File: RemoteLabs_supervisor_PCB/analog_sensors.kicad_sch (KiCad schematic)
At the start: 12 parts

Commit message: adding test sketch
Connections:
- net 5V_IN renamed VCC
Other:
- moved on the sheet: C?
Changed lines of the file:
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@@
     (stroke (width 0) (type default) (color 0 0 0 0))
   )
-  (wire (pts (xy 121.92 101.6) (xy 121.92 104.14))
+  (wire (pts (xy 121.92 102.87) (xy 121.92 104.14))
     (stroke (width 0) (type default) (color 0 0 0 0))
   )
@@
   )
   (wire (pts (xy 135.89 69.85) (xy 139.7 69.85))
+    (stroke (width 0) (type default) (color 0 0 0 0))
+  )
+  (wire (pts (xy 121.92 95.25) (xy 121.92 93.98))
     (stroke (width 0) (type default) (color 0 0 0 0))
   )
@@
     (effects (font (size 1.27 1.27)) (justify left bottom))
   )
-  (hierarchical_label "5V_IN" (shape input) (at 118.11 53.34 90)
+  (hierarchical_label "VCC" (shape input) (at 118.11 53.34 90)
     (effects (font (size 1.27 1.27)) (justify left))
   )
@@
     (pin "8")
   )
-  (symbol (lib_id "000_Capacitor_Film_Immo:cap_film_0805") (at 121.92 97.79 0) (unit 1)
-    (in_bom yes) (on_board yes) (fields_autoplaced)
-    (property "Reference" "C?" (id 0) (at 125.73 96.5199 0)
-      (effects (font (size 1.27 1.27)) (justify left))
-    )
-    (property "Value" "100n" (id 1) (at 125.73 99.0599 0)
-      (effects (font (size 1.27 1.27)) (justify left))
-    )
-    (property "Footprint" "Capacitor_SMD:C_0805_2012Metric_Pad1.18x1.45mm_HandSolder" (id 2) (at 123.19 107.95 0)
-      (effects (font (size 1.27 1.27)) hide)
-    )
-    (property "Datasheet" "~" (id 3) (at 121.92 97.79 0)
-      (effects (font (size 1.27 1.27)) hide)
-    )
+  (symbol (lib_id "000_Capacitor_Film_Immo:cap_film_0805") (at 121.92 99.06 0) (unit 1)
+    (in_bom yes) (on_board yes) (fields_autoplaced)
+    (property "Reference" "C?" (id 0) (at 125.73 97.7899 0)
+      (effects (font (size 1.27 1.27)) (justify left))
+    )
+    (property "Value" "100n" (id 1) (at 125.73 100.3299 0)
+      (effects (font (size 1.27 1.27)) (justify left))
+    )
+    (property "Footprint" "Capacitor_SMD:C_0805_2012Metric_Pad1.18x1.45mm_HandSolder" (id 2) (at 123.19 109.22 0)
+      (effects (font (size 1.27 1.27)) hide)
+    )
+    (property "Datasheet" "~" (id 3) (at 121.92 99.06 0)
+      (effects (font (size 1.27 1.27)) hide)
+    )

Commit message: V1.0 Circuit Design Complete
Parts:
- gave numbers to parts that had none: 12
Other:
- note added: "2.7 - 36v VCC"
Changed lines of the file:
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@@
   )
   (text "Table 5. Pin Function Descriptions\nPin No. Mnemonic Description\n1 −IN Negative Input.\n2 REF Reference. This pin must be driven by low impedance.\n3 −VS Negative Supply.\n4 NC No Connect.\n5 SENSE Sense Pin. In measurement mode, connect to output; in setpoint mode, connect to setpoint voltage.\n6 OUT Output.\n7 +VS Positive Supply.\n8 +IN Positive Input. "
-    (at 186.69 71.12 0)
+    (at 162.56 52.07 0)
     (effects (font (size 1.27 1.27)) (justify left bottom))
   )
@@
     (effects (font (size 0.8 0.8)) (justify left bottom))
   )
+  (text "2.7 - 36v VCC" (at 125.095 51.435 0)
+    (effects (font (size 1.27 1.27)) (justify left bottom))
+  )
   (text "Thermocouples / Temperature Sensing " (at 93.98 40.64 0)
     (effects (font (size 1.27 1.27)) (justify left bottom))
@@
   (symbol (lib_id "000_Capacitor_Film_Immo:cap_film_0805") (at 124.46 63.5 0) (unit 1)
     (in_bom yes) (on_board yes) (fields_autoplaced)
-    (property "Reference" "C?" (id 0) (at 128.27 62.2299 0)
+    (property "Reference" "C35" (id 0) (at 128.27 62.2299 0)
       (effects (font (size 1.27 1.27)) (justify left))
     )
@@
   (symbol (lib_id "000_Capacitor_Film_Immo:cap_film_0805") (at 102.87 82.55 0) (unit 1)
     (in_bom yes) (on_board yes) (fields_autoplaced)
-    (property "Reference" "C?" (id 0) (at 106.68 81.2799 0)
+    (property "Reference" "C32" (id 0) (at 106.68 81.2799 0)
       (effects (font (size 1.27 1.27)) (justify left))
     )
@@
   (symbol (lib_id "Connector:Screw_Terminal_01x02") (at 76.2 85.09 180) (unit 1)
     (in_bom yes) (on_board yes) (fields_autoplaced)
-    (property "Reference" "J?" (id 0) (at 76.2 76.2 0))
+    (property "Reference" "J22" (id 0) (at 76.2 76.2 0))
     (property "Value" "Thermocouple A" (id 1) (at 76.2 78.74 0))
     (property "Footprint" "" (id 2) (at 76.2 85.09 0)
@@
   (symbol (lib_id "000_Resistors_Immo:Resistor_0805") (at 86.36 92.71 0) (unit 1)
     (in_bom yes) (on_board yes) (fields_autoplaced)
-    (property "Reference" "R?" (id 0) (at 88.9 91.4399 0)
+    (property "Reference" "R14" (id 0) (at 88.9 91.4399 0)
       (effects (font (size 1.27 1.27)) (justify left))
     )
@@
   (symbol (lib_id "000_Capacitor_Electrolytic_Immo:22u") (at 137.16 99.06 0) (unit 1)
     (in_bom yes) (on_board yes) (fields_autoplaced)
-    (property "Reference" "C?" (id 0) (at 140.97 96.9009 0)
+    (property "Reference" "C37" (id 0) (at 140.97 96.9009 0)
       (effects (font (size 1.27 1.27)) (justify left))
     )
@@
   (symbol (lib_id "Sensor_Temperature:AD8497") (at 121.92 82.55 0) (unit 1)
     (in_bom yes) (on_board yes)
-    (property "Reference" "U?" (id 0) (at 125.73 76.2 0))
+    (property "Reference" "U19" (id 0) (at 125.73 76.2 0))
     (property "Value" "AD8497" (id 1) (at 128.27 78.74 0))
     (property "Footprint" "Package_SO:MSOP-8_3x3mm_P0.65mm" (id 2) (at 144.78 88.9 0)
@@
   (symbol (lib_id "000_Capacitor_Film_Immo:cap_film_0805") (at 121.92 99.06 0) (unit 1)
     (in_bom yes) (on_board yes) (fields_autoplaced)
-    (property "Reference" "C?" (id 0) (at 125.73 97.7899 0)
+    (property "Reference" "C34" (id 0) (at 125.73 97.7899 0)
       (effects (font (size 1.27 1.27)) (justify left))
     )
@@
   (symbol (lib_id "000_Resistors_Immo:Resistor_0805") (at 95.25 87.63 90) (unit 1)
     (in_bom yes) (on_board yes)
-    (property "Reference" "R?" (id 0) (at 95.25 81.28 90))
+    (property "Reference" "R16" (id 0) (at 95.25 81.28 90))
     (property "Value" "Resistor_0805" (id 1) (at 93.98 83.82 90))
     (property "Footprint" "Resistor_SMD:R_0805_2012Metric_Pad1.20x1.40mm_HandSolder" (id 2) (at 95.25 89.408 90)
@@
   (symbol (lib_id "000_Capacitor_Film_Immo:cap_film_0805") (at 102.87 92.71 0) (unit 1)
     (in_bom yes) (on_board yes) (fields_autoplaced)
-    (property "Reference" "C?" (id 0) (at 106.68 91.4399 0)
+    (property "Reference" "C33" (id 0) (at 106.68 91.4399 0)
       (effects (font (size 1.27 1.27)) (justify left))
     )
@@
   (symbol (lib_id "000_Capacitor_Film_Immo:cap_film_0805") (at 102.87 72.39 0) (unit 1)
     (in_bom yes) (on_board yes) (fields_autoplaced)
-    (property "Reference" "C?" (id 0) (at 106.68 71.1199 0)
+    (property "Reference" "C31" (id 0) (at 106.68 71.1199 0)
       (effects (font (size 1.27 1.27)) (justify left))
     )
@@
   (symbol (lib_id "000_Capacitor_Electrolytic_Immo:22u") (at 135.89 63.5 0) (unit 1)
     (in_bom yes) (on_board yes) (fields_autoplaced)
-    (property "Reference" "C?" (id 0) (at 139.7 61.3409 0)
+    (property "Reference" "C36" (id 0) (at 139.7 61.3409 0)
       (effects (font (size 1.27 1.27)) (justify left))
     )
@@
   (symbol (lib_id "000_Resistors_Immo:Resistor_0805") (at 93.98 77.47 90) (unit 1)
     (in_bom yes) (on_board yes)
-    (property "Reference" "R?" (id 0) (at 93.98 71.12 90))
+    (property "Reference" "R15" (id 0) (at 93.98 71.12 90))
     (property "Value" "Resistor_0805" (id 1) (at 92.71 73.66 90))
     (property "Footprint" "Resistor_SMD:R_0805_2012Metric_Pad1.20x1.40mm_HandSolder" (id 2) (at 93.98 79.248 90)

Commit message: Schematic reviewed
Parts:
- J22: footprint (none) -> TerminalBlock:TerminalBlock_Altech_AK300-2_P5.00mm
- R15, R16: value Resistor_0805 -> 10k
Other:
- note added: "Resistor Value Unknown Not On Datasheet. if R15 & R16 == 10k Corner frequency is ~160Hz. Is this suitable?"
- note removed: "Resistor Value Unknown Not On Datasheet. Work out RC Filter corner frequency?"
- moved on the sheet: C37
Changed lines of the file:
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@@
     (stroke (width 0) (type default) (color 0 0 0 0))
   )
-  (wire (pts (xy 124.46 93.98) (xy 137.16 93.98))
+  (wire (pts (xy 124.46 93.98) (xy 133.985 93.98))
     (stroke (width 0) (type default) (color 0 0 0 0))
   )
@@
     (stroke (width 0) (type default) (color 0 0 0 0))
   )
-  (wire (pts (xy 137.16 93.98) (xy 137.16 95.25))
+  (wire (pts (xy 133.985 93.98) (xy 133.985 95.25))
     (stroke (width 0) (type default) (color 0 0 0 0))
   )
@@
     (stroke (width 0) (type default) (color 0 0 0 0))
   )
-  (wire (pts (xy 137.16 102.87) (xy 137.16 104.14))
+  (wire (pts (xy 133.985 102.87) (xy 133.985 104.14))
     (stroke (width 0) (type default) (color 0 0 0 0))
   )
@@
     (stroke (width 0) (type default) (color 0 0 0 0))
   )
-  (wire (pts (xy 137.16 104.14) (xy 121.92 104.14))
+  (wire (pts (xy 133.985 104.14) (xy 121.92 104.14))
     (stroke (width 0) (type default) (color 0 0 0 0))
   )
@@
     )
   )
-  (text "Resistor Value\nUnknown\nNot On Datasheet.\n\nWork out RC Filter corner frequency?\n"
-    (at 60.96 60.96 0)
+  (text "Resistor Value\nUnknown\nNot On Datasheet.\n\nif R15 & R16 == 10k\n\nCorner frequency is ~160Hz. Is this suitable?\n"
+    (at 65.405 66.675 0)
     (effects (font (size 0.8 0.8)) (justify left bottom))
   )
@@
     (property "Reference" "J22" (id 0) (at 76.2 76.2 0))
     (property "Value" "Thermocouple A" (id 1) (at 76.2 78.74 0))
-    (property "Footprint" "" (id 2) (at 76.2 85.09 0)
+    (property "Footprint" "TerminalBlock:TerminalBlock_Altech_AK300-2_P5.00mm" (id 2) (at 76.2 85.09 0)
       (effects (font (size 1.27 1.27)) hide)
     )
@@
     (pin "2")
   )
-  (symbol (lib_id "000_Capacitor_Electrolytic_Immo:22u") (at 137.16 99.06 0) (unit 1)
-    (in_bom yes) (on_board yes) (fields_autoplaced)
-    (property "Reference" "C37" (id 0) (at 140.97 96.9009 0)
-      (effects (font (size 1.27 1.27)) (justify left))
-    )
-    (property "Value" "10u" (id 1) (at 140.97 99.4409 0)
-      (effects (font (size 1.27 1.27)) (justify left))
-    )
-    (property "Footprint" "Capacitor_SMD:CP_Elec_6.3x5.9" (id 2) (at 138.1252 102.87 0)
-      (effects (font (size 1.27 1.27)) hide)
-    )
-    (property "Datasheet" "~" (id 3) (at 137.16 99.06 0)
+  (symbol (lib_id "000_Capacitor_Electrolytic_Immo:22u") (at 133.985 99.06 0) (unit 1)
+    (in_bom yes) (on_board yes) (fields_autoplaced)
+    (property "Reference" "C37" (id 0) (at 137.795 96.9009 0)
+      (effects (font (size 1.27 1.27)) (justify left))
+    )
+    (property "Value" "10u" (id 1) (at 137.795 99.4409 0)
+      (effects (font (size 1.27 1.27)) (justify left))
+    )
+    (property "Footprint" "Capacitor_SMD:CP_Elec_6.3x5.9" (id 2) (at 134.9502 102.87 0)
+      (effects (font (size 1.27 1.27)) hide)
+    )
+    (property "Datasheet" "~" (id 3) (at 133.985 99.06 0)
       (effects (font (size 1.27 1.27)) hide)
     )
@@
   (symbol (lib_id "000_Resistors_Immo:Resistor_0805") (at 95.25 87.63 90) (unit 1)
     (in_bom yes) (on_board yes)
-    (property "Reference" "R16" (id 0) (at 95.25 81.28 90))
-    (property "Value" "Resistor_0805" (id 1) (at 93.98 83.82 90))
+    (property "Reference" "R16" (id 0) (at 93.98 83.185 90))
+    (property "Value" "10k" (id 1) (at 93.98 85.09 90))
     (property "Footprint" "Resistor_SMD:R_0805_2012Metric_Pad1.20x1.40mm_HandSolder" (id 2) (at 95.25 89.408 90)
       (effects (font (size 1.27 1.27)) hide)
@@
     (in_bom yes) (on_board yes)
     (property "Reference" "R15" (id 0) (at 93.98 71.12 90))
-    (property "Value" "Resistor_0805" (id 1) (at 92.71 73.66 90))
+    (property "Value" "10k" (id 1) (at 92.71 73.66 90))
     (property "Footprint" "Resistor_SMD:R_0805_2012Metric_Pad1.20x1.40mm_HandSolder" (id 2) (at 93.98 79.248 90)
       (effects (font (size 1.27 1.27)) hide)

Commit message: mbncmvbc,
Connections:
- net GND_A: now also R14.1; no longer R14.2
- net at C31.2, C32.1, U19.8 (+IN): now also R15.1; no longer R15.2
- net at C32.2, C33.1, U19.1 (-IN): now also R16.1; no longer R16.2
- net at J22.2 (Pin_2): now also R15.2; no longer R15.1
- new net: J22.1 (Pin_1), R14.2, R16.2
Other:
- moved on the sheet: R14, R15, R16
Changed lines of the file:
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@@
     (pin "2")
   )
-  (symbol (lib_id "000_Resistors_Immo:Resistor_0805") (at 86.36 92.71 0) (unit 1)
-    (in_bom yes) (on_board yes) (fields_autoplaced)
-    (property "Reference" "R14" (id 0) (at 88.9 91.4399 0)
-      (effects (font (size 1.27 1.27)) (justify left))
+  (symbol (lib_id "000_Resistors_Immo:Resistor_0805") (at 86.36 92.71 90) (unit 1)
+    (in_bom yes) (on_board yes)
+    (property "Reference" "R14" (id 0) (at 88.265 91.44 90)
+      (effects (font (size 1.27 1.27)) (justify right))
     )
-    (property "Value" "1M" (id 1) (at 88.9 93.9799 0)
-      (effects (font (size 1.27 1.27)) (justify left))
+    (property "Value" "1M" (id 1) (at 88.265 93.98 90)
+      (effects (font (size 1.27 1.27)) (justify right))
     )
-    (property "Footprint" "Resistor_SMD:R_0805_2012Metric_Pad1.20x1.40mm_HandSolder" (id 2) (at 84.582 92.71 90)
+    (property "Footprint" "Resistor_SMD:R_0805_2012Metric_Pad1.20x1.40mm_HandSolder" (id 2) (at 86.36 94.488 90)
       (effects (font (size 1.27 1.27)) hide)
     )
@@
     (pin "2")
   )
-  (symbol (lib_id "000_Resistors_Immo:Resistor_0805") (at 95.25 87.63 90) (unit 1)
+  (symbol (lib_id "000_Resistors_Immo:Resistor_0805") (at 95.25 87.63 180) (unit 1)
     (in_bom yes) (on_board yes)
-    (property "Reference" "R16" (id 0) (at 93.98 83.185 90))
-    (property "Value" "10k" (id 1) (at 93.98 85.09 90))
-    (property "Footprint" "Resistor_SMD:R_0805_2012Metric_Pad1.20x1.40mm_HandSolder" (id 2) (at 95.25 89.408 90)
+    (property "Reference" "R16" (id 0) (at 93.98 85.09 0))
+    (property "Value" "10k" (id 1) (at 95.25 87.63 0))
+    (property "Footprint" "Resistor_SMD:R_0805_2012Metric_Pad1.20x1.40mm_HandSolder" (id 2) (at 97.028 87.63 90)
       (effects (font (size 1.27 1.27)) hide)
     )
@@
     (pin "2")
   )
-  (symbol (lib_id "000_Resistors_Immo:Resistor_0805") (at 93.98 77.47 90) (unit 1)
+  (symbol (lib_id "000_Resistors_Immo:Resistor_0805") (at 93.98 77.47 180) (unit 1)
     (in_bom yes) (on_board yes)
-    (property "Reference" "R15" (id 0) (at 93.98 71.12 90))
-    (property "Value" "10k" (id 1) (at 92.71 73.66 90))
-    (property "Footprint" "Resistor_SMD:R_0805_2012Metric_Pad1.20x1.40mm_HandSolder" (id 2) (at 93.98 79.248 90)
+    (property "Reference" "R15" (id 0) (at 93.345 74.93 0))
+    (property "Value" "10k" (id 1) (at 93.98 77.47 0))
+    (property "Footprint" "Resistor_SMD:R_0805_2012Metric_Pad1.20x1.40mm_HandSolder" (id 2) (at 95.758 77.47 90)
       (effects (font (size 1.27 1.27)) hide)
     )

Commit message: Footprint Association Underway
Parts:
- renumbered C37 to EC7, C36 to EC8
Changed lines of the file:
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@@
   (symbol (lib_id "000_Capacitor_Electrolytic_Immo:22u") (at 133.985 99.06 0) (unit 1)
     (in_bom yes) (on_board yes) (fields_autoplaced)
-    (property "Reference" "C37" (id 0) (at 137.795 96.9009 0)
+    (property "Reference" "EC7" (id 0) (at 137.795 96.9009 0)
       (effects (font (size 1.27 1.27)) (justify left))
     )
@@
   (symbol (lib_id "000_Capacitor_Electrolytic_Immo:22u") (at 135.89 63.5 0) (unit 1)
     (in_bom yes) (on_board yes) (fields_autoplaced)
-    (property "Reference" "C36" (id 0) (at 139.7 61.3409 0)
+    (property "Reference" "EC8" (id 0) (at 139.7 61.3409 0)
       (effects (font (size 1.27 1.27)) (justify left))
     )

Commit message: Footprint associations complete
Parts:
- EC7, EC8: footprint Capacitor_SMD:CP_Elec_6.3x5.9 -> Capacitor_SMD:CP_Elec_4x5.4
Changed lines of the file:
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@@
       (effects (font (size 1.27 1.27)) (justify left))
     )
-    (property "Footprint" "Capacitor_SMD:CP_Elec_6.3x5.9" (id 2) (at 134.9502 102.87 0)
+    (property "Footprint" "Capacitor_SMD:CP_Elec_4x5.4" (id 2) (at 134.9502 102.87 0)
       (effects (font (size 1.27 1.27)) hide)
     )
@@
       (effects (font (size 1.27 1.27)) (justify left))
     )
-    (property "Footprint" "Capacitor_SMD:CP_Elec_6.3x5.9" (id 2) (at 136.8552 67.31 0)
+    (property "Footprint" "Capacitor_SMD:CP_Elec_4x5.4" (id 2) (at 136.8552 67.31 0)
       (effects (font (size 1.27 1.27)) hide)
     )

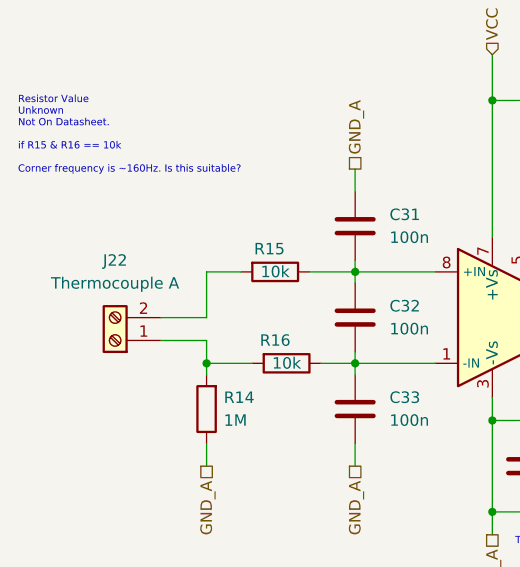
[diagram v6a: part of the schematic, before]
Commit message: Edited PCB design for V1.1
- Changed pin sizes for stepper motor
- Change pin sizes for DC/DC Buck module.
- In process of changing text to be readable by human beings
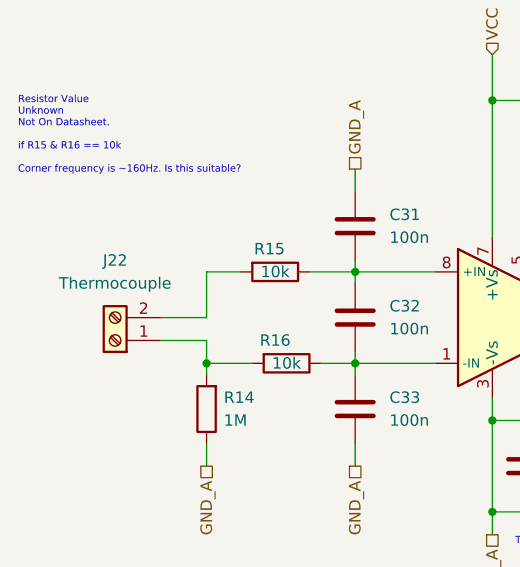
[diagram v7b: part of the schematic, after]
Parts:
- J22: value Thermocouple A -> Thermocouple
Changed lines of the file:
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@@
     (in_bom yes) (on_board yes) (fields_autoplaced)
     (property "Reference" "J22" (id 0) (at 76.2 76.2 0))
-    (property "Value" "Thermocouple A" (id 1) (at 76.2 78.74 0))
+    (property "Value" "Thermocouple" (id 1) (at 76.2 78.74 0))
     (property "Footprint" "TerminalBlock:TerminalBlock_Altech_AK300-2_P5.00mm" (id 2) (at 76.2 85.09 0)
       (effects (font (size 1.27 1.27)) hide)
